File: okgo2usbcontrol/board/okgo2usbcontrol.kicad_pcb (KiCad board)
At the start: 2 copper layers, 22 parts, among them IC1 ADP3335, IC2 STM32F042K6T6, P1 USB-A, P2 SWD_TC, P3 COAX, SW1 FIRE, SW2 ARM, U1 RFM95W

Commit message: Very initial placement ideas
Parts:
- D2, P1, P3, U1: moved to F.Cu
- IC1, IC2, P2: moved to B.Cu
- moved P3 64.0 mm to (137.5, 112.5), turned to 270 degrees
- moved U1 63.9 mm to (126.2, 112.5), turned to 90 degrees
- moved IC2 63.7 mm to (120.0, 112.5)
- moved P1 63.5 mm to (102.8, 112.5), turned to 270 degrees
- moved D2 62.6 mm to (136.2, 105.2), turned to 0 degrees
- moved SW2 61.3 mm to (110.0, 121.8)
- moved P2 57.2 mm to (110.5, 109.6), turned to 180 degrees
- moved D1 32.8 mm to (110.2, 117.5), turned to 180 degrees
- moved SW1 24.7 mm to (111.5, 104.0), turned to 270 degrees
- moved IC1 20.5 mm to (109.5, 104.5), turned to 180 degrees
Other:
- board outline added: 40 x 25 mm

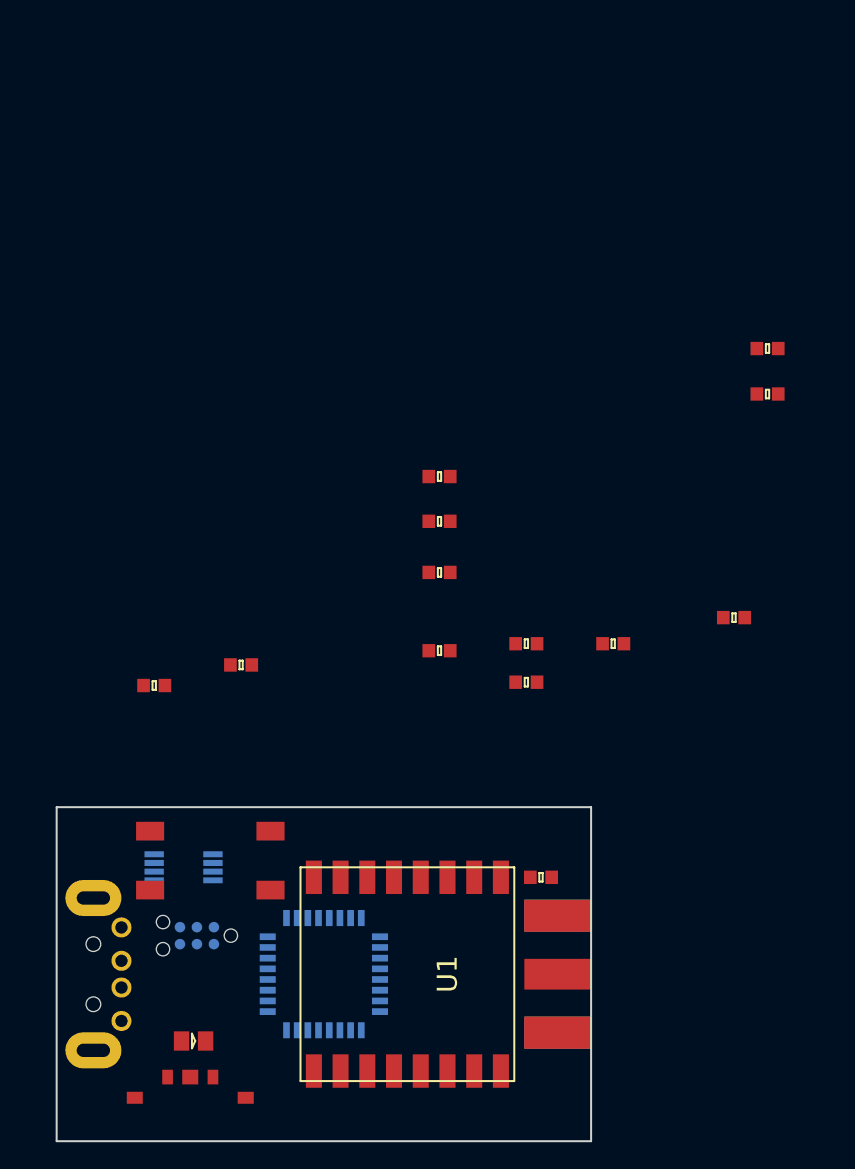
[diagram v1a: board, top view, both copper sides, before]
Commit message: Tweak usbcontrol into silly dongle board
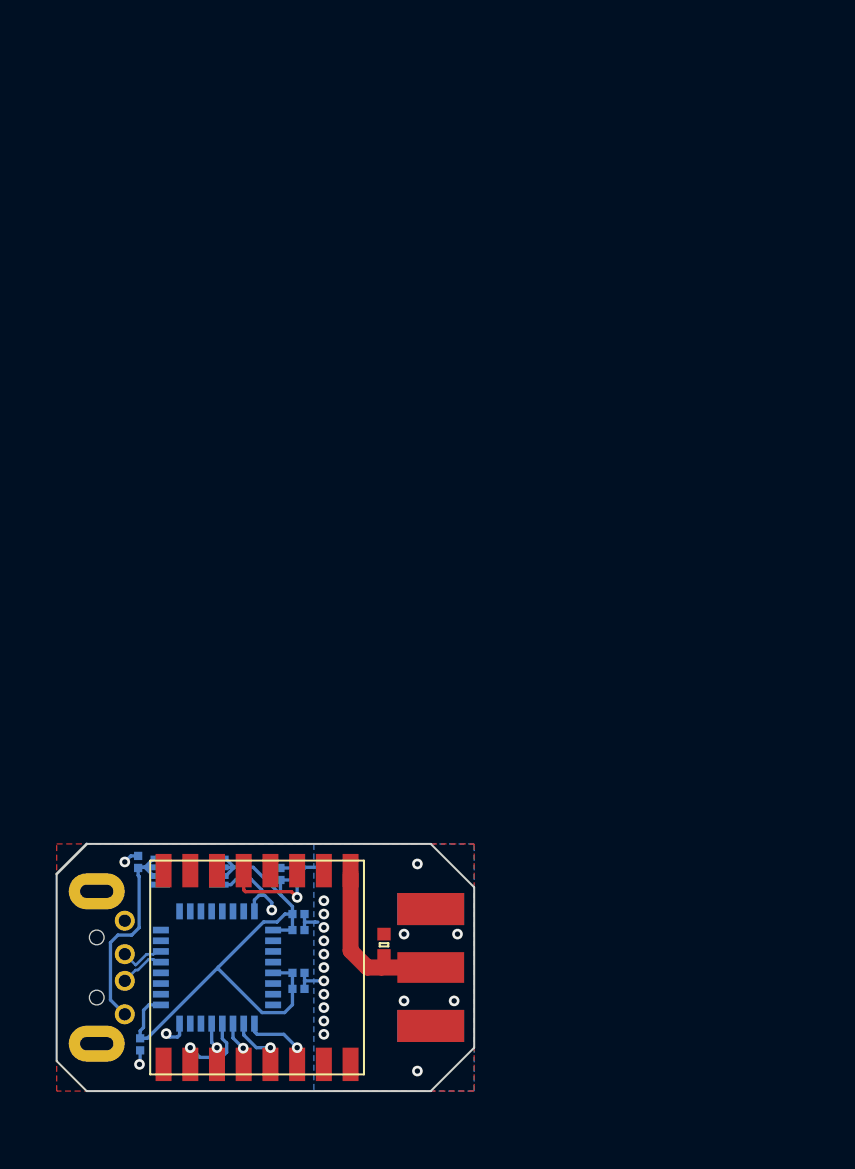
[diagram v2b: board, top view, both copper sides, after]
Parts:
- removed D1: LED_bicolour, agg:0805-LED
- removed P2: SWD_TC, agg:TC2030-NL
- removed R1, R2: 10k, agg:0603
- removed R3: R, agg:0603
- removed SW1: FIRE, footprints:FSM2JSMx
- removed SW2: ARM, footprints:JSX08001SAQNL
- C1, C2, C3, C4, C5, C6, C7, C8, C9: footprint agg:0603 -> agg:0402; moved to B.Cu
- moved C7 58.4 mm to (118.1, 112.4)
- moved C9 50.3 mm to (118.0, 105.0), turned to 90 degrees
- moved C4 41.8 mm to (106.2, 117.8), turned to 270 degrees
- moved C2 39.8 mm to (118.1, 113.6)
- moved C8 39.0 mm to (116.8, 105.0), turned to 90 degrees
- moved C3 31.2 mm to (118.1, 108.0)
- moved C6 23.4 mm to (118.1, 109.2)
- moved C1 15.6 mm to (114.0, 105.0), turned to 270 degrees
- moved C5 13.3 mm to (106.1, 104.1), turned to 90 degrees
- moved D2 12.8 mm to (124.5, 110.3), turned to 90 degrees
- moved U1 11.3 mm to (115.0, 112.0)
- moved P3 9.51 mm to (128.0, 112.0)
- moved IC2 8.02 mm to (112.0, 112.0)
- moved P1 0.56 mm to (103.0, 112.0)
- moved IC1 0.56 mm to (110.0, 104.8)
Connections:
- IC2 pad 10: Net-(IC2-Pad10) -> /RFM_NSS
- IC2 pad 11: Net-(IC2-Pad11) -> /RFM_SCK
- IC2 pad 12: Net-(IC2-Pad12) -> /RFM_MISO
- IC2 pad 13: Net-(IC2-Pad13) -> /RFM_MOSI
- IC2 pad 23: /SWDIO -> Net-(IC2-Pad23)
- IC2 pad 24: /SWDCLK -> Net-(IC2-Pad24)
- IC2 pad 30: /BOOT -> Net-(IC2-Pad30)
- IC2 pad 31: /BOOT -> Net-(IC2-Pad31)
- IC2 pad 4: /nRST -> Net-(IC2-Pad4)
- IC2 pad 9: Net-(IC2-Pad9) -> /RFM_RESET
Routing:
- net +3V3: track 0.00 -> 51.9 mm, vias 0 -> 1
- net GND: track 0.00 -> 20.4 mm, vias 0 -> 21
- net Net-(C5-Pad1): track 0.00 -> 17.9 mm
- net Net-(D2-Pad1): track 0.00 -> 13.4 mm
- net /RFM_MISO: track 0.00 -> 6.46 mm, vias 0 -> 1
- net /RFM_RESET: track 0.00 -> 5.30 mm, vias 0 -> 1
- net /RFM_NSS: track 0.00 -> 4.24 mm, vias 0 -> 1
- net /USB_D+: track 0.00 -> 3.45 mm
- net /USB_D-: track 0.00 -> 3.45 mm
- net /RFM_SCK: track 0.00 -> 3.13 mm, vias 0 -> 1
- net /RFM_MOSI: track 0.00 -> 2.97 mm, vias 0 -> 1
- added copper zone on B.Cu, net GND
- added copper zone on F.Cu, net GND
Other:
- board size 40 x 25 mm -> 31.2 x 18.5 mm
- net class ANT added: clearance 0.8, trace_width 0.25, via_dia 0.8, via_drill 0.4
- rule pad_to_mask_clearance: 0.2 -> 0

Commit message: WIP
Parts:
- added R1: 100K, agg:0402, B.Cu at (107.8, 99.9)
- added W1: BOOT, agg:TESTPAD, B.Cu at (107.5, 107.5)
- added W2: 3v3, agg:TESTPAD, B.Cu at (113.4, 99.7)
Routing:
- net Net-(IC2-Pad31): track 0.00 -> 7.92 mm
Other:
- net class Default: clearance 0.2 -> 0
- rule trace_clearance: 0.2 -> 0
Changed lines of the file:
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@@
-(kicad_pcb (version 20170123) (host pcbnew no-vcs-found-a20cce0~59~ubuntu16.04.1)
+(kicad_pcb (version 20170123) (host pcbnew "(2017-08-19 revision a20cce0)-master")
   (general
     (thickness 1.6)
     (drawings 8)
-    (tracks 161)
+    (tracks 165)
     (zones 0)
-    (modules 15)
+    (modules 18)
     (nets 40)
   )
@@
     (user_trace_width 1)
     (user_trace_width 1.2)
-    (trace_clearance 0.2)
+    (trace_clearance 0)
     (zone_clearance 0.508)
     (zone_45_only no)
@@
   (net 39 "Net-(IC2-Pad31)")
   (net_class Default "This is the default net class."
-    (clearance 0.2)
+    (clearance 0)
     (trace_width 0.25)
     (via_dia 0.8)
@@
     (uvia_drill 0.1)
     (add_net "Net-(D2-Pad1)")
+  )
+  (module agg:0402 (layer B.Cu)
+    (at 107.7675 99.874344)
+    (fp_text reference R1 (at -1.71 0 -90) (layer B.Fab)
+      (effects (font (size 1 1) (thickness 0.15)) (justify mirror))
+    )
+    (fp_text value 100K (at 1.71 0 -90) (layer B.Fab)
+      (effects (font (size 1 1) (thickness 0.15)) (justify mirror))
+    )
+    (fp_line (start -0.5 0.25) (end 0.5 0.25) (layer B.Fab) (width 0.01))
+    (fp_line (start 0.5 0.25) (end 0.5 -0.25) (layer B.Fab) (width 0.01))
+    (fp_line (start 0.5 -0.25) (end -0.5 -0.25) (layer B.Fab) (width 0.01))
+    (fp_line (start -0.5 -0.25) (end -0.5 0.25) (layer B.Fab) (width 0.01))
+    (fp_line (start -0.2 0.25) (end -0.2 -0.25) (layer B.Fab) (width 0.01))
+    (fp_line (start 0.2 0.25) (end 0.2 -0.25) (layer B.Fab) (width 0.01))
+    (fp_line (start -1.05 0.6) (end 1.05 0.6) (layer B.CrtYd) (width 0.01))
+    (fp_line (start 1.05 0.6) (end 1.05 -0.6) (layer B.CrtYd) (width 0.01))
+    (fp_line (start 1.05 -0.6) (end -1.05 -0.6) (layer B.CrtYd) (width 0.01))
+    (fp_line (start -1.05 -0.6) (end -1.05 0.6) (layer B.CrtYd) (width 0.01))
+    (pad 1 smd rect (at -0.45 0) (size 0.62 0.62) (layers B.Cu B.Paste B.Mask)
+      (net 39 "Net-(IC2-Pad31)"))
+    (pad 2 smd rect (at 0.45 0) (size 0.62 0.62) (layers B.Cu B.Paste B.Mask)
+      (net 4 GND))
+    (model ${KISYS3DMOD}/Resistors_SMD.3dshapes/R_0402.wrl
+      (at (xyz 0 0 0))
+      (scale (xyz 1 1 1))
+      (rotate (xyz 0 0 0))
+    )
+  )
+  (module agg:TESTPAD (layer B.Cu)
+    (at 113.378333 99.720416)
+    (fp_text reference W2 (at 0 1.4) (layer B.Fab) hide
+      (effects (font (size 1 1) (thickness 0.15)) (justify mirror))
+    )
+    (fp_text value 3v3 (at 0 -1.6) (layer B.Fab) hide
+      (effects (font (size 1 1) (thickness 0.15)) (justify mirror))
+    )
+    (fp_line (start -0.75 -0.75) (end 0.75 -0.75) (layer B.CrtYd) (width 0.01))
+    (fp_line (start -0.75 0.75) (end -0.75 -0.75) (layer B.CrtYd) (width 0.01))
+    (fp_line (start 0.75 0.75) (end -0.75 0.75) (layer B.CrtYd) (width 0.01))
+    (fp_line (start 0.75 -0.75) (end 0.75 0.75) (layer B.CrtYd) (width 0.01))
+    (pad 1 smd circle (at 0 0) (size 1 1) (layers B.Cu B.Mask)
+      (net 15 +3V3))
+  )
+  (module agg:TESTPAD (layer B.Cu)
+    (at 107.5 107.5)
+    (fp_text reference W1 (at 0 1.4) (layer B.Fab) hide
+      (effects (font (size 1 1) (thickness 0.15)) (justify mirror))
+    )
+    (fp_text value BOOT (at 0 -1.6) (layer B.Fab) hide
+      (effects (font (size 1 1) (thickness 0.15)) (justify mirror))
+    )
+    (fp_line (start -0.75 -0.75) (end 0.75 -0.75) (layer B.CrtYd) (width 0.01))
+    (fp_line (start -0.75 0.75) (end -0.75 -0.75) (layer B.CrtYd) (width 0.01))
+    (fp_line (start 0.75 0.75) (end -0.75 0.75) (layer B.CrtYd) (width 0.01))
+    (fp_line (start 0.75 -0.75) (end 0.75 0.75) (layer B.CrtYd) (width 0.01))
+    (pad 1 smd circle (at 0 0) (size 1 1) (layers B.Cu B.Mask)
+      (net 39 "Net-(IC2-Pad31)"))
   )
   (module agg:0402 (layer B.Cu)
@@
   (segment (start 113.25 104.5) (end 113.25 104.45) (width 0.25) (layer B.Cu) (net 15))
   (segment (start 113.25 104.45) (end 112.65 103.85) (width 0.25) (layer B.Cu) (net 15))
+  (segment (start 114 107.8) (end 114 107) (width 0.25) (layer B.Cu) (net 39))
+  (segment (start 114 107) (end 113.5 106.5) (width 0.25) (layer B.Cu) (net 39))
+  (segment (start 113.5 106.5) (end 108.5 106.5) (width 0.25) (layer B.Cu) (net 39))
+  (segment (start 108.5 106.5) (end 107.5 107.5) (width 0.25) (layer B.Cu) (net 39))
   (zone (net 4) (net_name GND) (layer F.Cu) (hatch edge 0.508)
     (connect_pads (clearance 0.508))

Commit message: WIP
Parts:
- W1, W2: footprint agg:TESTPAD -> footprints:PokyPad
- moved W2 17.0 mm to (116.4, 116.4)
- moved R1 9.57 mm to (115.2, 105.9), turned to 90 degrees
- moved C8 0.81 mm to (117.2, 104.3)
- moved C9 0.81 mm to (118.4, 104.3)
- moved W1 0.14 mm to (107.6, 107.6)
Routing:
- net +3V3: track 51.9 -> 54.4 mm
- net Net-(IC2-Pad31): track 7.92 -> 9.12 mm
